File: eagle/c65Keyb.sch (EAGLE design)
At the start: 94 parts, among them Q1 8Mhz, U1 STM32F407IET6__FI__, U2 744245, U3 744245, U4 744245, X4 MKDS_5/3-6,35

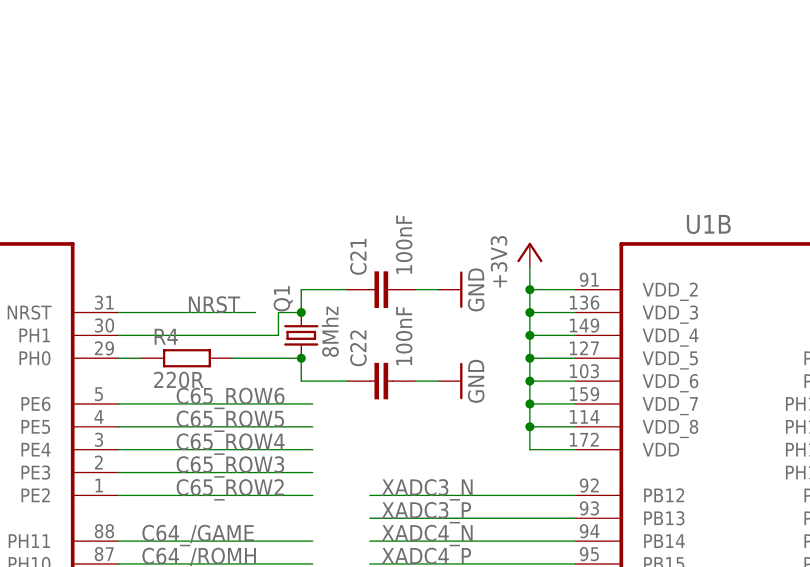
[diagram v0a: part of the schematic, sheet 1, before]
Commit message: added LED support and updated the eagle schematics
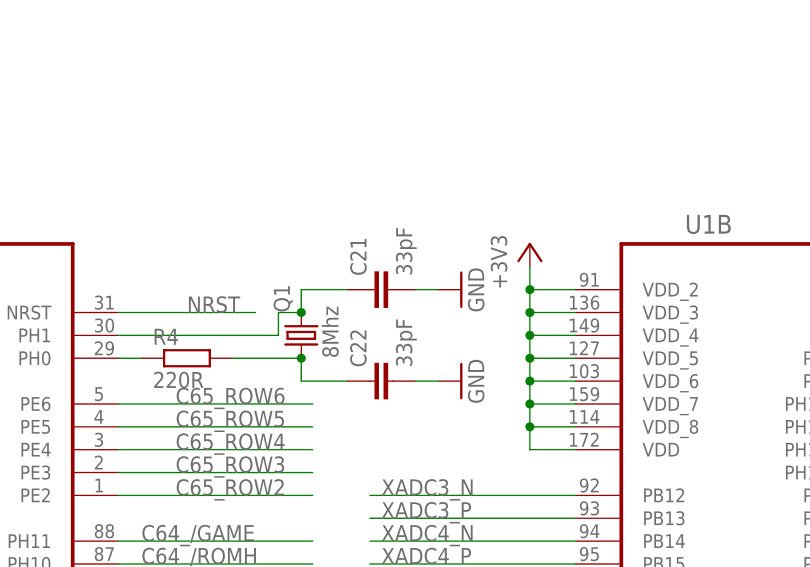
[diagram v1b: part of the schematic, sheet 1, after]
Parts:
- C21, C22: value 100nF -> 33pF
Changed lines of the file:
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@@
 <?xml version="1.0" encoding="utf-8"?>
 <!DOCTYPE eagle SYSTEM "eagle.dtd">
-<eagle version="7.2.0">
+<eagle version="7.1.0">
 <drawing>
 <settings>
@@
 <setting verticaltext="up"/>
 </settings>
-<grid distance="50" unitdist="mil" unit="mil" style="lines" multiple="1" display="no" altdistance="0.01" altunitdist="inch" altunit="inch"/>
+<grid distance="0.1" unitdist="inch" unit="inch" style="lines" multiple="1" display="no" altdistance="0.01" altunitdist="inch" altunit="inch"/>
 <layers>
 <layer number="1" name="Top" color="4" fill="1" visible="no" active="no"/>
@@
 <part name="+3V4" library="supply1" deviceset="+3V3" device=""/>
 <part name="Q1" library="fi-CRYSTAL" deviceset="CRYSTAL" device="-HC49UP" value="8Mhz"/>
-<part name="C21" library="rcl" deviceset="C-EU" device="C0805" value="100nF"/>
-<part name="C22" library="rcl" deviceset="C-EU" device="C0805" value="100nF"/>
+<part name="C21" library="rcl" deviceset="C-EU" device="C0805" value="33pF"/>
+<part name="C22" library="rcl" deviceset="C-EU" device="C0805" value="33pF"/>
 <part name="GND7" library="supply1" deviceset="GND" device=""/>
 <part name="GND8" library="supply1" deviceset="GND" device=""/>
